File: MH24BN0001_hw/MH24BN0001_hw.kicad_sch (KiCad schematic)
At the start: 2 parts, among them J1 ST-Link V2 Header

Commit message: previous commit
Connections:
- net NRST: now also STM32WB55Cx2.7 (NRST)
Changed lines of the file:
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@@
+	(wire
+		(pts
+			(xy 74.93 44.45) (xy 83.82 44.45)
+		)
+		(stroke
+			(width 0)
+			(type default)
+		)
+	)
 	(wire
 		(pts
@@
 			(width 0)
 			(type default)
+		)
+	)
+	(label "NRST"
+		(at 74.93 44.45 0)
+		(fields_autoplaced yes)
+		(effects
+			(font
+				(size 1.27 1.27)
+			)
+			(justify left bottom)
 		)
 	)
@@
 			)
 		)
-		(property "Datasheet" ""
+		(property "Datasheet" "https://www.st.com/resource/en/datasheet/stm32wb55cc.pdf"
 			(at 96.52 38.1 0)
 			(effects

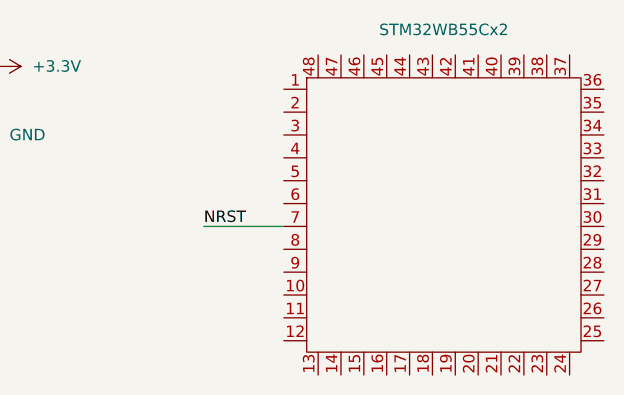
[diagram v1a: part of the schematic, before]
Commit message: Changing chip to STM32F401RB
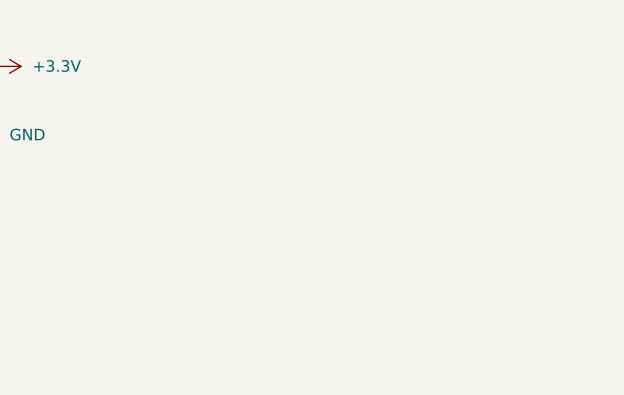
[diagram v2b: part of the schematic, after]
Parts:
- removed STM32WB55Cx2: ~, symbol Sym_lib:STM32WB55CC
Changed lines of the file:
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@@
-	(wire
-		(pts
-			(xy 74.93 44.45) (xy 83.82 44.45)
-		)
-		(stroke
-			(width 0)
-			(type default)
-		)
-	)
 	(wire
 		(pts
@@
 			(width 0)
 			(type default)
-		)
-	)
-	(label "NRST"
-		(at 74.93 44.45 0)
-		(fields_autoplaced yes)
-		(effects
-			(font
-				(size 1.27 1.27)
-			)
-			(justify left bottom)
 		)
 	)
@@
 					(unit 1)
 				)
-			)
-		)
-	)
-	(symbol
-		(lib_name "STM32WB55CC_1")
-		(lib_id "Sym_lib:STM32WB55CC")
-		(at 101.6 44.45 0)
-		(unit 1)
-		(exclude_from_sim no)
-		(in_bom yes)
-		(on_board yes)
-		(dnp no)
-		(property "Reference" "STM32WB55Cx2"
-			(at 101.6 22.606 0)
-			(effects
-				(font
-					(size 1.27 1.27)
-				)
-			)
-		)
-		(property "Value" "~"
-			(at 125.73 26.0665 0)
-			(effects
-				(font
-					(size 1.27 1.27)
-				)
-			)
-		)
-		(property "Footprint" ""
-			(at 96.52 38.1 0)
-			(effects
-				(font
-					(size 1.27 1.27)
-				)
-				(hide yes)
-			)
-		)
-		(property "Datasheet" "https://www.st.com/resource/en/datasheet/stm32wb55cc.pdf"
-			(at 96.52 38.1 0)
-			(effects
-				(font
-					(size 1.27 1.27)
-				)
-				(hide yes)
-			)
-		)
-		(property "Description" ""
-			(at 96.52 38.1 0)
-			(effects
-				(font
-					(size 1.27 1.27)
-				)
-				(hide yes)
-			)
-		)
-		(pin "16"
-		)
-		(pin "1"
-		)
-		(pin "20"
-		)
-		(pin "29"
-		)
-		(pin "32"
-		)
-		(pin "5"
-		)
-		(pin "38"
-		)
-		(pin "26"
-		)
-		(pin "11"
-		)
-		(pin "12"
-		)
-		(pin "14"
-		)
-		(pin "30"
-		)
-		(pin "27"
-		)
-		(pin "13"
-		)
-		(pin "2"
-		)
-		(pin "25"
-		)
-		(pin "31"
-		)
-		(pin "3"
-		)
-		(pin "17"
-		)
-		(pin "19"
-		)
-		(pin "22"
-		)
-		(pin "24"
-		)
-		(pin "21"
-		)
-		(pin "18"
-		)
-		(pin "28"
-		)
-		(pin "33"
-		)
-		(pin "23"
-		)
-		(pin "34"
-		)
-		(pin "35"
-		)
-		(pin "36"
-		)
-		(pin "10"
-		)
-		(pin "37"
-		)
-		(pin "15"
-		)
-		(pin "8"
-		)
-		(pin "4"
-		)
-		(pin "43"
-		)
-		(pin "7"
-		)
-		(pin "9"
-		)
-		(pin "40"
-		)
-		(pin "46"
-		)
-		(pin "41"
-		)
-		(pin "42"
-		)
-		(pin "44"
-		)
-		(pin "45"
-		)
-		(pin "47"
-		)
-		(pin "39"
-		)
-		(pin "48"
-		)
-		(pin "6"
-		)
-		(instances
-			(project ""
-				(path "/1e9f19f6-5b3f-4aa5-b603-02119a5ead72"
-					(reference "STM32WB55Cx2")
-					(unit 1)
-				)

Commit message: previous commit
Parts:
- added U1: STM32F401RBT6, Library:QFP50P1200X1200X160-64N, symbol Sym_lib:STM32F401RBT6
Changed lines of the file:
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@@
+	)
+	(symbol
+		(lib_id "Sym_lib:STM32F401RBT6")
+		(at 218.44 92.71 0)
+		(unit 1)
+		(exclude_from_sim no)
+		(in_bom yes)
+		(on_board yes)
+		(dnp no)
+		(fields_autoplaced yes)
+		(property "Reference" "U1"
+			(at 218.44 16.51 0)
+			(effects
+				(font
+					(size 1.27 1.27)
+				)
+			)
+		)
+		(property "Value" "STM32F401RBT6"
+			(at 218.44 19.05 0)
+			(effects
+				(font
+					(size 1.27 1.27)
+				)
+			)
+		)
+		(property "Footprint" "Library:QFP50P1200X1200X160-64N"
+			(at 218.44 92.71 0)
+			(effects
+				(font
+					(size 1.27 1.27)
+				)
+				(justify bottom)
+				(hide yes)
+			)
+		)
+		(property "Datasheet" "https://www.st.com/content/ccc/resource/technical/document/datasheet/9e/50/b1/5a/5f/ae/4d/c1/DM00086815.pdf/files/DM00086815.pdf/jcr:content/translations/en.DM00086815.pdf"
+			(at 218.44 92.71 0)
+			(effects
+				(font
+					(size 1.27 1.27)
+				)
+				(hide yes)
+			)
+		)
+		(property "Description" ""
+			(at 218.44 92.71 0)
+			(effects
+				(font
+					(size 1.27 1.27)
+				)
+				(hide yes)
+			)
+		)
+		(property "MANUFACTURER" "STMicroelectronics"
+			(at 218.44 92.71 0)
+			(effects
+				(font
+					(size 1.27 1.27)
+				)
+				(justify bottom)
+				(hide yes)
+			)
+		)
+		(pin "43"
+		)
+		(pin "44"
+		)
+		(pin "13"
+		)
+		(pin "1"
+		)
+		(pin "11"
+		)
+		(pin "19"
+		)
+		(pin "30"
+		)
+		(pin "33"
+		)
+		(pin "17"
+		)
+		(pin "34"
+		)
+		(pin "2"
+		)
+		(pin "16"
+		)
+		(pin "21"
+		)
+		(pin "3"
+		)
+		(pin "26"
+		)
+		(pin "22"
+		)
+		(pin "27"
+		)
+		(pin "12"
+		)
+		(pin "35"
+		)
+		(pin "36"
+		)
+		(pin "15"
+		)
+		(pin "40"
+		)
+		(pin "37"
+		)
+		(pin "14"
+		)
+		(pin "10"
+		)
+		(pin "41"
+		)
+		(pin "38"
+		)
+		(pin "29"
+		)
+		(pin "24"
+		)
+		(pin "42"
+		)
+		(pin "18"
+		)
+		(pin "23"
+		)
+		(pin "28"
+		)
+		(pin "31"
+		)
+		(pin "32"
+		)
+		(pin "20"
+		)
+		(pin "25"
+		)
+		(pin "39"
+		)
+		(pin "4"
+		)
+		(pin "49"
+		)
+		(pin "52"
+		)
+		(pin "55"
+		)
+		(pin "64"
+		)
+		(pin "9"
+		)
+		(pin "60"
+		)
+		(pin "7"
+		)
+		(pin "62"
+		)
+		(pin "56"
+		)
+		(pin "47"
+		)
+		(pin "63"
+		)
+		(pin "45"
+		)
+		(pin "5"
+		)
+		(pin "50"
+		)
+		(pin "6"
+		)
+		(pin "48"
+		)
+		(pin "46"
+		)
+		(pin "57"
+		)
+		(pin "53"
+		)
+		(pin "8"
+		)
+		(pin "51"
+		)
+		(pin "61"
+		)
+		(pin "58"
+		)
+		(pin "59"
+		)
+		(pin "54"
+		)
+		(instances
+			(project ""
+				(path "/1e9f19f6-5b3f-4aa5-b603-02119a5ead72"
+					(reference "U1")
+					(unit 1)
+				)
+			)
+		)
 	)
 	(symbol

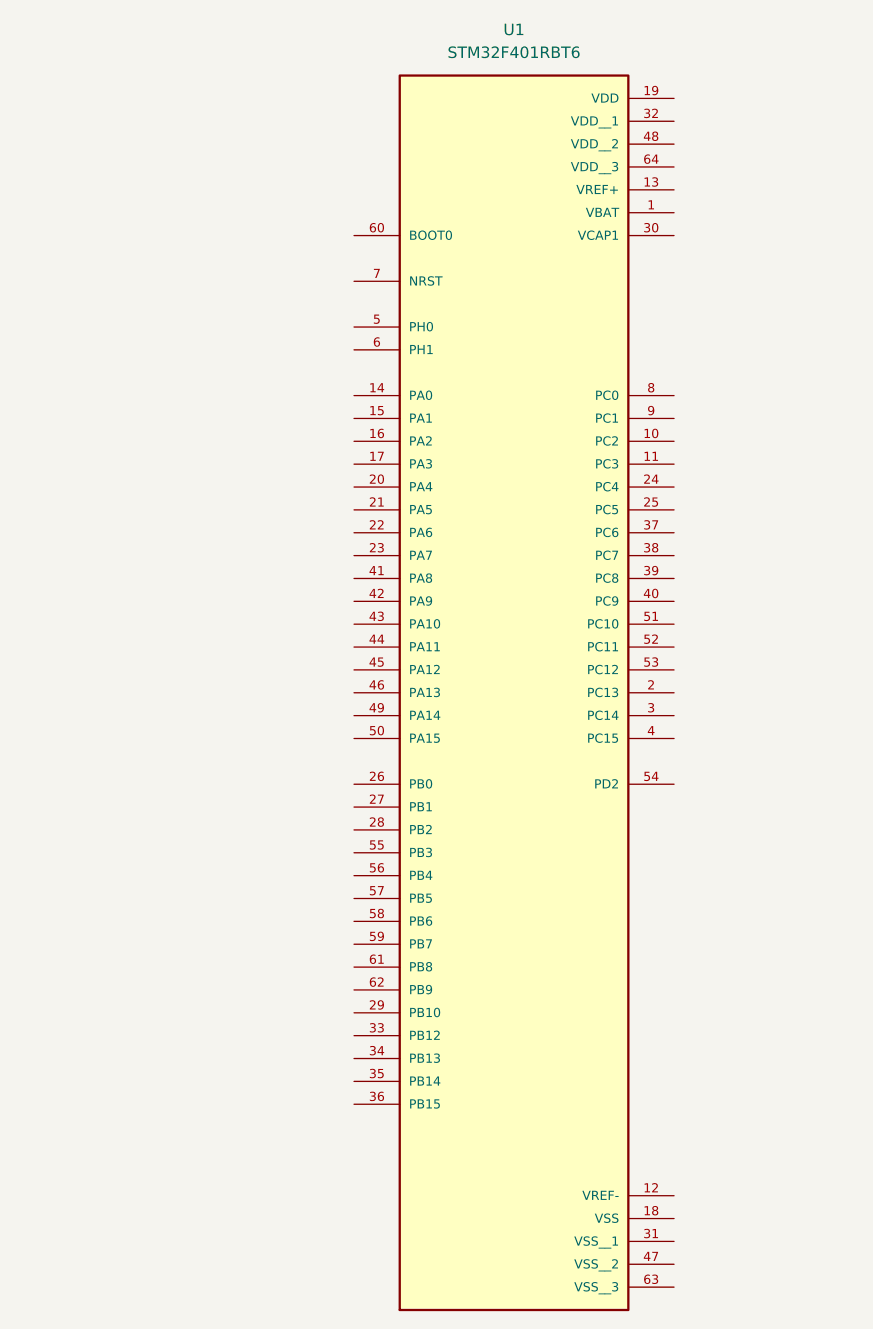
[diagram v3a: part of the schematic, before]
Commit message: Adding essential pin functions to STM32F4
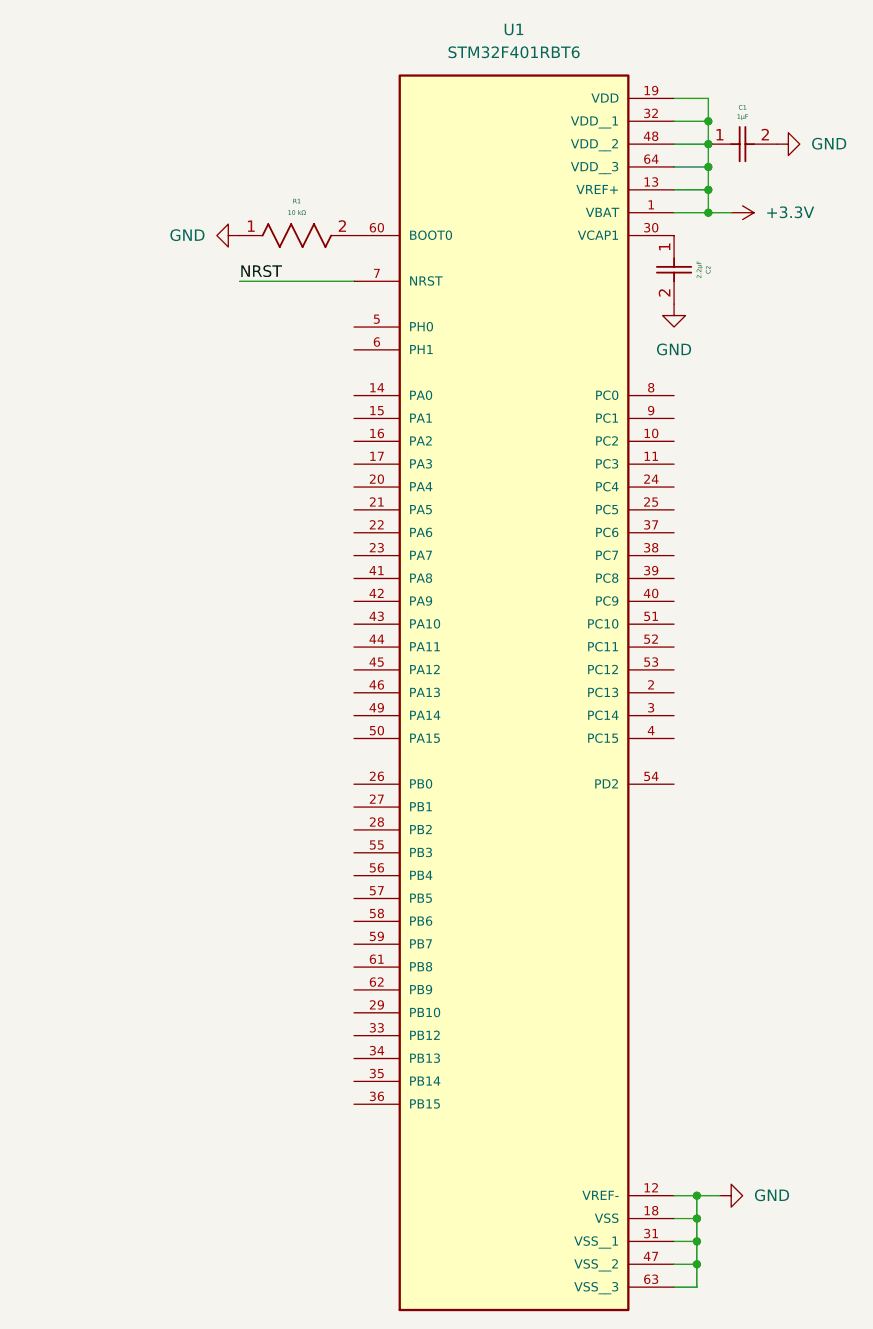
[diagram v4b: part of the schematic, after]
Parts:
- added C1: 1µF, Library:1µF_cap, symbol Sym_lib:CL10B105KP8NNNC
- added C2: 2.2µF, Library:2.2µF_cap, symbol Sym_lib:CL10A225KO8NNNC
- added R1: 10 kΩ, Library:10 kΩ, symbol Sym_lib:CF14JT10K0
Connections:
- net +3.3V: now also U1.1 (VBAT), U1.13 (VREF+), U1.19 (VDD), U1.32 (VDD__1), U1.48 (VDD__2), U1.64 (VDD__3), C1.1
- net GND: now also U1.12 (VREF-), U1.18 (VSS), U1.31 (VSS__1), U1.47 (VSS__2), U1.63 (VSS__3), C1.2, C2.2, R1.1
- net NRST: now also U1.7 (NRST)
- net at U1.30 (VCAP1): now also C2.1
- net at U1.60 (BOOT0): now also R1.2

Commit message: Adding SWDIO and SWCLK
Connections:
- net SWCLK: now also U1.49 (PA14)
- net SWDIO: now also U1.46 (PA13)
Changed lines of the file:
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@@
+	(wire
+		(pts
+			(xy 190.5 92.71) (xy 200.66 92.71)
+		)
+		(stroke
+			(width 0)
+			(type default)
+		)
+	)
 	(wire
 		(pts
@@
 	(wire
 		(pts
+			(xy 190.5 90.17) (xy 200.66 90.17)
+		)
+		(stroke
+			(width 0)
+			(type default)
+		)
+	)
+	(wire
+		(pts
 			(xy 236.22 31.75) (xy 240.03 31.75)
 		)
@@
 			(width 0)
 			(type default)
+		)
+	)
+	(label "SWDIO"
+		(at 190.5 90.17 0)
+		(fields_autoplaced yes)
+		(effects
+			(font
+				(size 1.27 1.27)
+			)
+			(justify left bottom)
 		)
 	)
@@
 		(fields_autoplaced yes)
 		(effects
+			(font
+				(size 1.27 1.27)
+			)
+			(justify left bottom)
+		)
+	)
+	(label "SWCLK"
+		(at 190.5 92.71 0)
+		(fields_autoplaced yes)
+		(effects

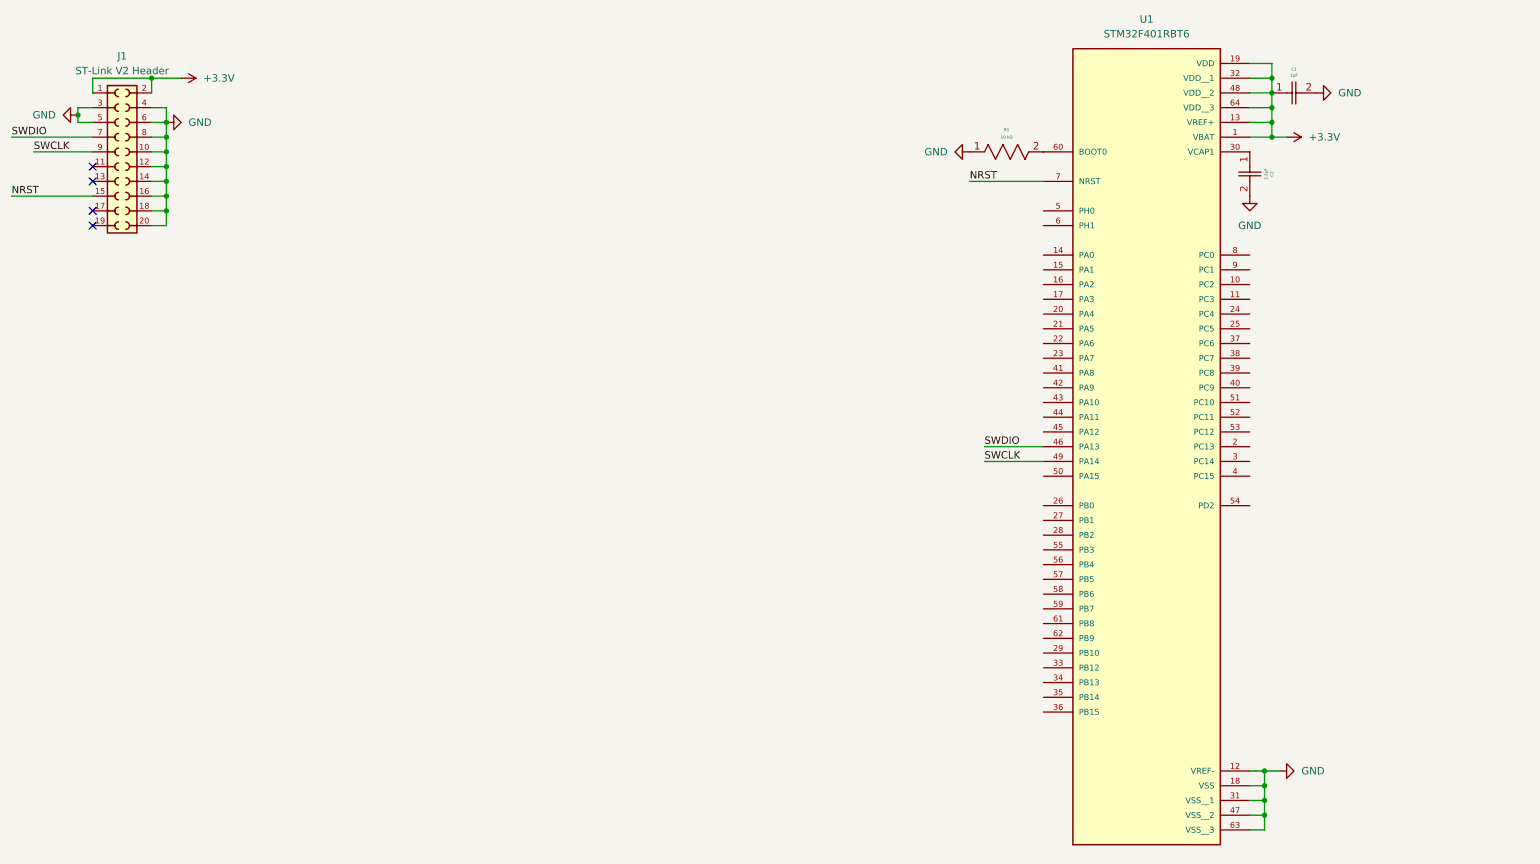
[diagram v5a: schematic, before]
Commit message: Adding serial interface to board, finishing schematic
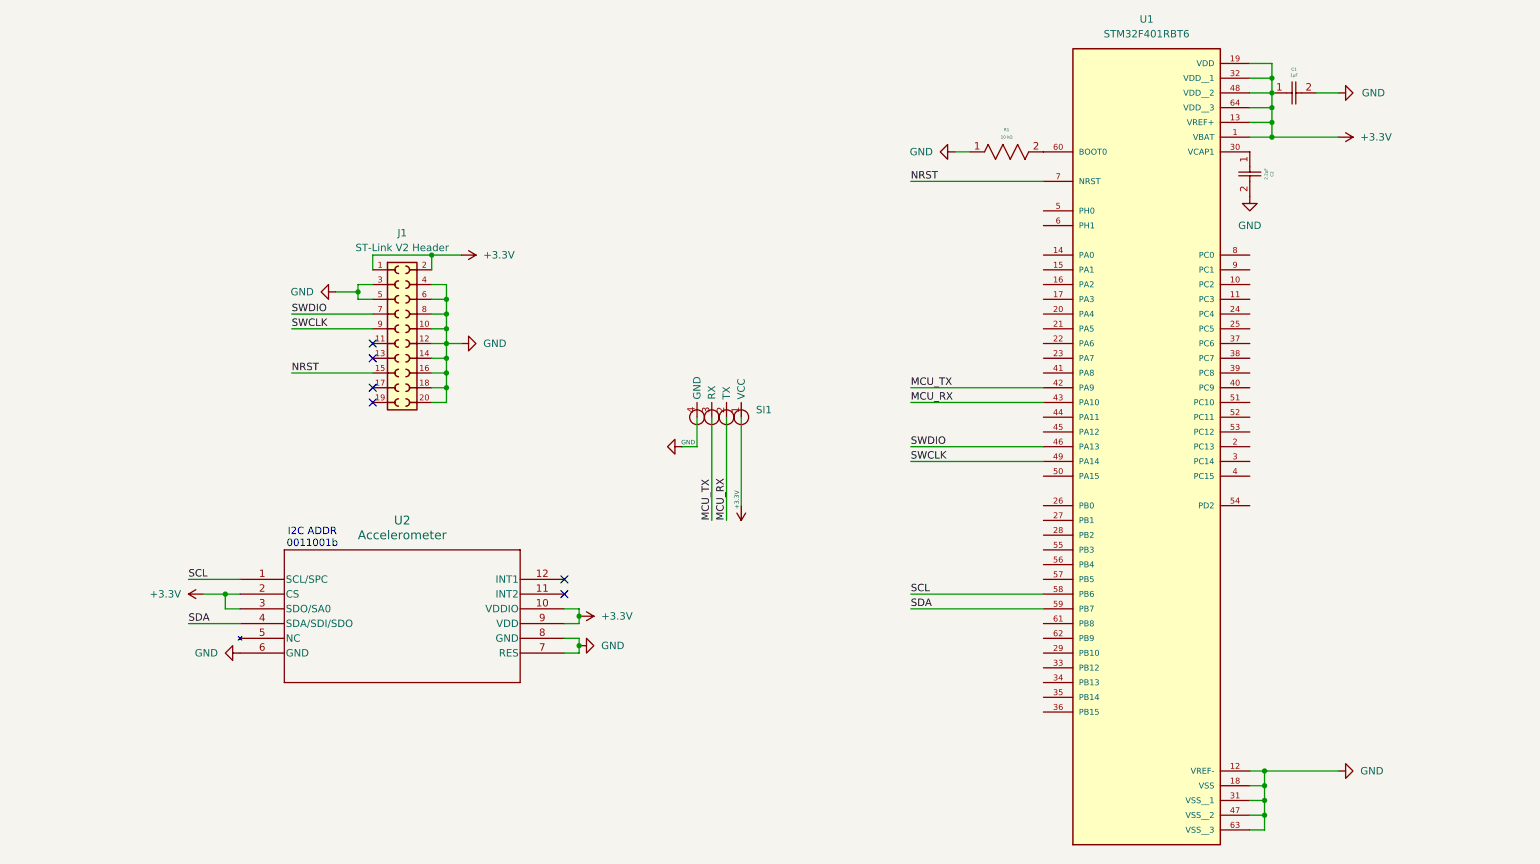
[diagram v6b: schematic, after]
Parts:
- added SI1: ~, Library:serial_interface, symbol Sym_lib:Serial_Interface
- added U2: Accelerometer, Library:acc, symbol Sym_lib:LIS2DTW12TR
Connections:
- net +3.3V: now also SI1.1 (VCC), U2.10 (VDDIO), U2.2 (CS), U2.3 (SDO/SA0), U2.9 (VDD)
- net GND: now also SI1.4 (GND), U2.6 (GND), U2.7 (RES), U2.8 (GND)
- net MCU_TX: now reaches U1.42 (PA9)
- net MCU_TX: now also SI1.3 (RX)
- net MCU_RX: now reaches U1.43 (PA10)
- net MCU_RX: now also SI1.2 (TX)
- net SCL: now reaches U1.58 (PB6)
- net SCL: now also U2.1 (SCL/SPC)
- net SDA: now reaches U1.59 (PB7)
- net SDA: now also U2.4 (SDA/SDI/SDO)
- no-connect marks 4 -> 6
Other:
- note added: "I2C ADDR 0011001b"
- moved on the sheet: J1

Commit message: starting PCB
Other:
- note added: "Serial"
- moved on the sheet: C1, C2, J1, R1, SI1, U1, U2

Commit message: finishing pcb, generating output files
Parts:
- added C1, C2, C4, C5, C6: 1µF, Library:1µF_cap, symbol Sym_lib:CL10B105KP8NNNC
- renumbered C1 to C3, C2 to C7
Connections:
- net +3.3V: now also C1.1, C2.1, C4.1, C5.1, C6.1
- net GND: now also C1.2, C2.2, C4.2, C5.2, C6.2
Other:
- moved on the sheet: C3
